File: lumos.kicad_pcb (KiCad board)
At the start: 2 copper layers, 35.6 x 21.6 mm, 8 parts, among them CON1 BARREL_JACK, IC1 ATTINY85-P, P1 LDP8806, P2 SPI, SW1 SW_PUSH

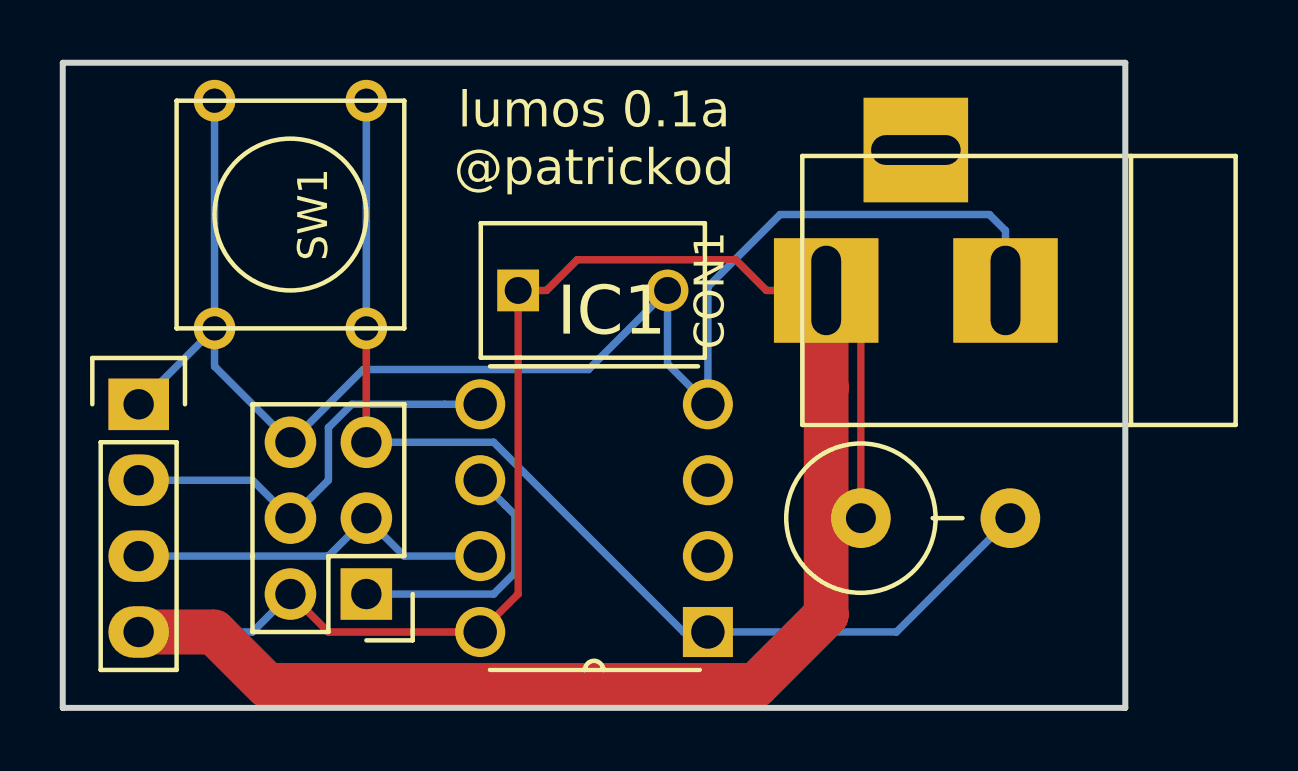
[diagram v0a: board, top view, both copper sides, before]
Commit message: Finalized v0.1a with output gerber assets
lumos-v0.1a-2016-02-04.zip contains the gerber assets sent to OSHPark
for printing.
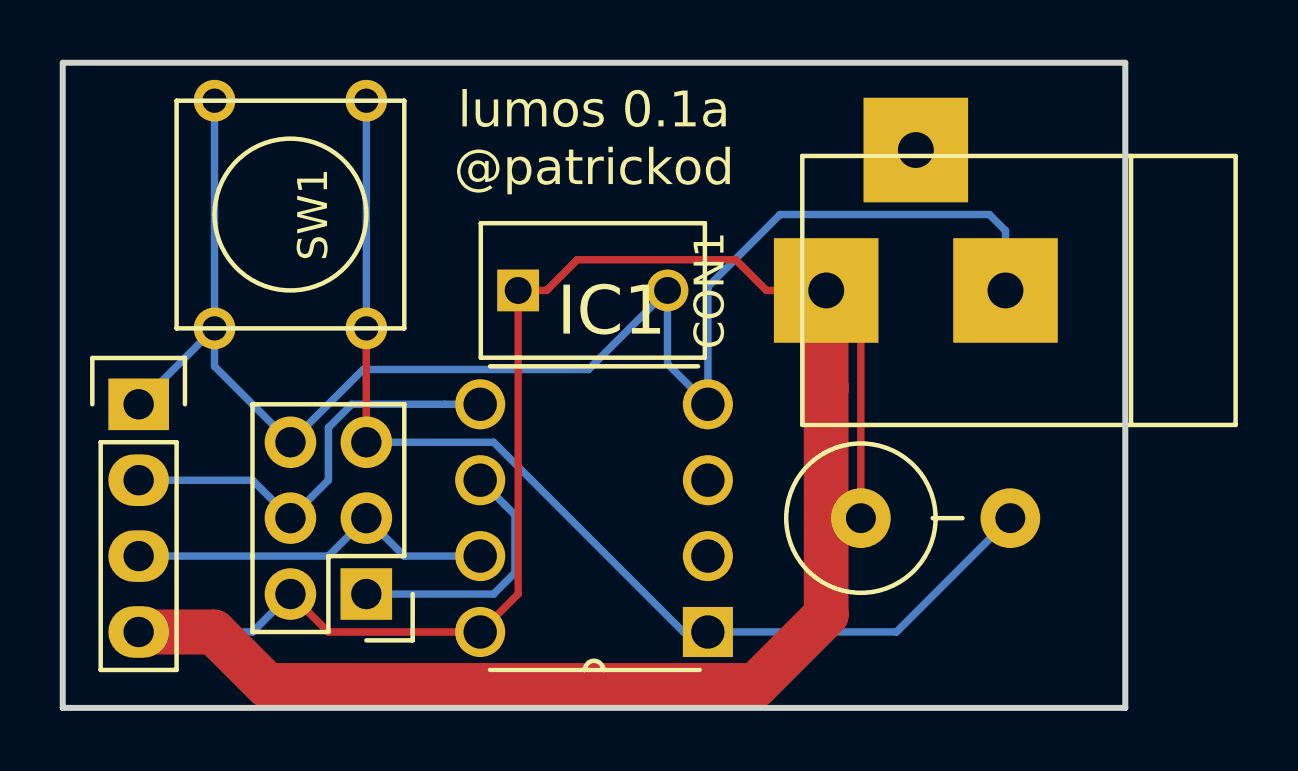
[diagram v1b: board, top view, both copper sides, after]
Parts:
- moved REF** 3.81 mm to (153.7, 95.2)
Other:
- board text added: "v0.1a 2016-02-04 GPLv3"
- board text removed: "v0.1a 2/4/16 GPLv3"
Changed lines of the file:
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@@
     (links 21)
     (no_connects 0)
-    (area 134.893076 89.78348 175.368021 117.3018)
+    (area 135.789999 92.609999 171.550001 114.400001)
     (thickness 1.6)
     (drawings 6)
@@
     (mod_text_size 1 1)
     (mod_text_width 0.15)
-    (pad_size 1.5 1.5)
-    (pad_drill 0.6)
+    (pad_size 3.50012 3.50012)
+    (pad_drill 1.2)
     (pad_to_mask_clearance 0)
     (aux_axis_origin 0 0)
     (visible_elements FFFFFF7F)
     (pcbplotparams
-      (layerselection 0x00030_80000001)
-      (usegerberextensions false)
+      (layerselection 0x010f0_80000001)
+      (usegerberextensions true)
       (excludeedgelayer true)
       (linewidth 0.100000)
@@
       (outputformat 1)
       (mirror false)
-      (drillshape 1)
+      (drillshape 0)
       (scaleselection 1)
-      (outputdirectory ""))
+      (outputdirectory oshpark/))
   )
   (net 0 "")
@@
     (fp_line (start 7.00024 4.50088) (end 7.00024 -4.50088) (layer F.SilkS) (width 0.15))
     (fp_line (start 7.00024 -4.50088) (end -7.50062 -4.50088) (layer F.SilkS) (width 0.15))
-    (pad 1 thru_hole rect (at 6.20014 0 180) (size 3.50012 3.50012) (drill oval 1.00076 2.99974) (layers *.Cu *.Mask F.SilkS)
+    (pad 1 thru_hole rect (at 6.20014 0 180) (size 3.50012 3.50012) (drill 1.2) (layers *.Cu *.Mask F.SilkS)
       (net 1 +5V))
-    (pad 2 thru_hole rect (at 0.20066 0 180) (size 3.50012 3.50012) (drill oval 1.00076 2.99974) (layers *.Cu *.Mask F.SilkS)
-      (net 2 GND))
-    (pad 3 thru_hole rect (at 3.2004 4.699 180) (size 3.50012 3.50012) (drill oval 2.99974 1.00076) (layers *.Cu *.Mask F.SilkS)
+    (pad 2 thru_hole rect (at 0.20066 0 180) (size 3.50012 3.50012) (drill 1.2) (layers *.Cu *.Mask F.SilkS)
+      (net 2 GND))
+    (pad 3 thru_hole rect (at 3.2004 4.699 180) (size 3.50012 3.50012) (drill 1.2) (layers *.Cu *.Mask F.SilkS)
       (net 2 GND))
   )
   (module Symbols:Symbol_OSHW-Logo_SilkScreen locked (layer Bottom)
-    (at 157.48 95.25 180)
+    (at 153.67 95.25 180)
     (descr "Symbol, OSHW-Logo, Silk Screen,")
     (tags "Symbol, OSHW-Logo, Silk Screen,")
@@
     (fp_line (start 0.35052 -0.89916) (end 0.7493 -1.89992) (layer B.SilkS) (width 0.15))
   )
-  (gr_text "v0.1a\n2/4/16\nGPLv3" (at 151.13 95.25) (layer B.SilkS)
+  (gr_text "v0.1a\n2016-02-04\nGPLv3" (at 143.51 97.79) (layer B.SilkS)
     (effects (font (size 1 1) (thickness 0.1)) (justify mirror))
   )
